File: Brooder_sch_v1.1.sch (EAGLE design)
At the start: 30 parts, among them J1 DCJ0202, J2 1X2-3.5MM, U1 328P

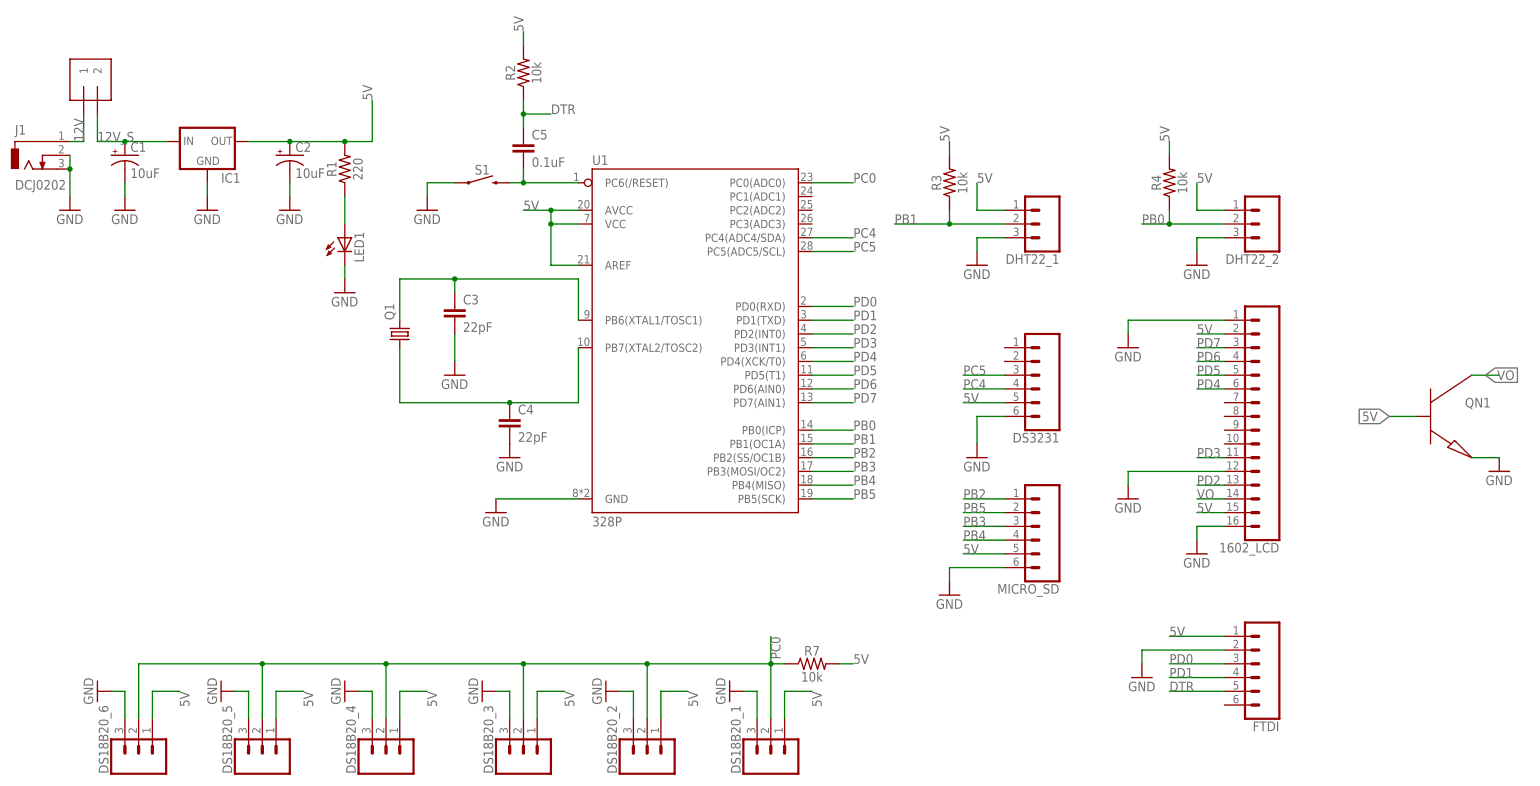
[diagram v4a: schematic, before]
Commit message: Adds test led
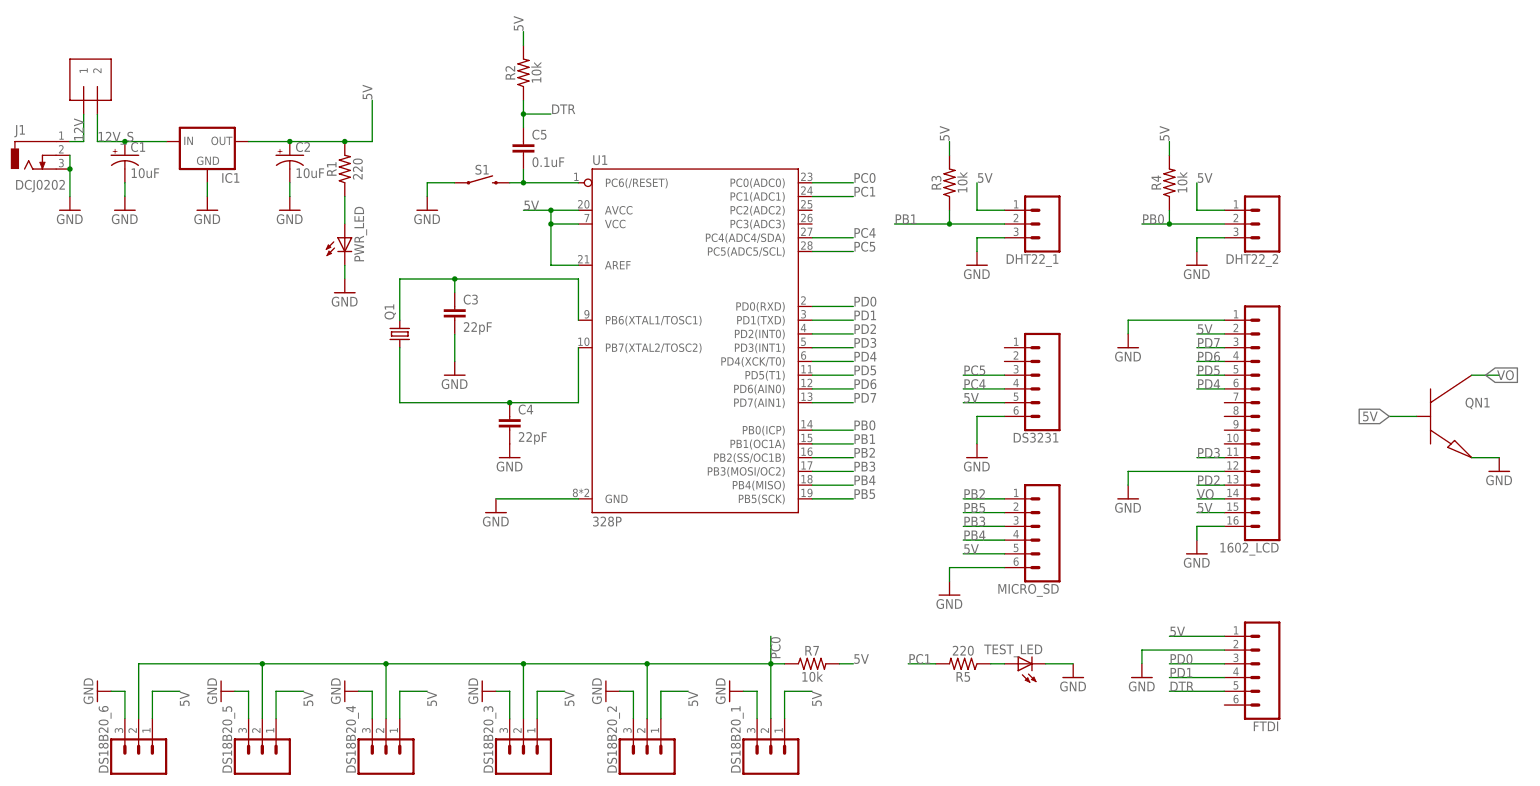
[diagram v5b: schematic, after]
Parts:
- added R5: 220, SparkFun-Resistors:10MOHM-HORIZ-1/4W-5%
- added TEST_LED: (no value), adafruit:LED5MM
- renumbered LED1 to PWR_LED
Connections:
- new net N$1: R5.1, TEST_LED.A
- new net PC1: R5.2, U1.PC1(ADC1)
- net GND: now also TEST_LED.C
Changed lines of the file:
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@@
 <part name="IC1" library="v-reg" library_urn="urn:adsk.eagle:library:409" deviceset="78XXS" device="" package3d_urn="urn:adsk.eagle:package:30342/1"/>
 <part name="R1" library="SparkFun-Resistors" deviceset="10MOHM" device="-HORIZ-1/4W-5%" value="220"/>
-<part name="LED1" library="adafruit" deviceset="LED" device="5MM"/>
+<part name="PWR_LED" library="adafruit" deviceset="LED" device="5MM"/>
 <part name="U1" library="SparkFun-IC-Microcontroller" deviceset="ATMEGA328P_PDIP" device="" value="328P"/>
 <part name="Q1" library="adafruit" deviceset="CRYSTAL" device="HC49S"/>
@@
 <part name="DS3231" library="SparkFun-Connectors" deviceset="CONN_06" device="NO_SILK_FEMALE_PTH"/>
 <part name="GND24" library="supply1" library_urn="urn:adsk.eagle:library:371" deviceset="GND" device=""/>
+<part name="R5" library="SparkFun-Resistors" deviceset="10MOHM" device="-HORIZ-1/4W-5%" value="220"/>
+<part name="TEST_LED" library="adafruit" deviceset="LED" device="5MM"/>
+<part name="GND25" library="supply1" library_urn="urn:adsk.eagle:library:371" deviceset="GND" device=""/>
 </parts>
 <sheets>
@@
 <attribute name="VALUE" x="-8.636" y="106.68" size="1.778" layer="96" font="vector" rot="R90" align="top-center"/>
 </instance>
-<instance part="LED1" gate="G$1" x="-10.16" y="93.98" smashed="yes">
+<instance part="PWR_LED" gate="G$1" x="-10.16" y="93.98" smashed="yes">
 <attribute name="NAME" x="-6.604" y="89.408" size="1.778" layer="95" rot="R90"/>
 <attribute name="VALUE" x="-4.445" y="89.408" size="1.778" layer="96" rot="R90"/>
@@
 <instance part="GND24" gate="1" x="106.68" y="53.34" smashed="yes">
 <attribute name="VALUE" x="104.14" y="50.8" size="1.778" layer="96"/>
+</instance>
+<instance part="R5" gate="G$1" x="104.14" y="15.24" smashed="yes" rot="R180">
+<attribute name="NAME" x="104.14" y="13.716" size="1.778" layer="95" font="vector" rot="R180" align="bottom-center"/>
+<attribute name="VALUE" x="104.14" y="16.764" size="1.778" layer="96" font="vector" rot="R180" align="top-center"/>
+</instance>
+<instance part="TEST_LED" gate="G$1" x="114.3" y="15.24" smashed="yes" rot="R90">
+<attribute name="NAME" x="118.872" y="18.796" size="1.778" layer="95" rot="R180"/>
+<attribute name="VALUE" x="118.872" y="20.955" size="1.778" layer="96" rot="R180"/>
+</instance>
+<instance part="GND25" gate="1" x="124.46" y="12.7" smashed="yes">
+<attribute name="VALUE" x="121.92" y="10.16" size="1.778" layer="96"/>
 </instance>
 </instances>
@@
 </segment>
 <segment>
-<pinref part="LED1" gate="G$1" pin="C"/>
+<pinref part="PWR_LED" gate="G$1" pin="C"/>
 <pinref part="GND5" gate="1" pin="GND"/>
 <wire x1="-10.16" y1="88.9" x2="-10.16" y2="86.36" width="0.1524" layer="91"/>
@@
 <wire x1="106.68" y1="60.96" x2="106.68" y2="55.88" width="0.1524" layer="91"/>
 <pinref part="GND24" gate="1" pin="GND"/>
+</segment>
+<segment>
+<pinref part="TEST_LED" gate="G$1" pin="C"/>
+<pinref part="GND25" gate="1" pin="GND"/>
+<wire x1="119.38" y1="15.24" x2="124.46" y2="15.24" width="0.1524" layer="91"/>
 </segment>
 </net>
@@
 <segment>
 <pinref part="R1" gate="G$1" pin="1"/>
-<pinref part="LED1" gate="G$1" pin="A"/>
+<pinref part="PWR_LED" gate="G$1" pin="A"/>
 <wire x1="-10.16" y1="101.6" x2="-10.16" y2="96.52" width="0.1524" layer="91"/>
 </segment>
@@
 </segment>
 </net>
+<net name="N$1" class="0">
+<segment>
+<pinref part="R5" gate="G$1" pin="1"/>
+<pinref part="TEST_LED" gate="G$1" pin="A"/>
+<wire x1="109.22" y1="15.24" x2="111.76" y2="15.24" width="0.1524" layer="91"/>
+</segment>
+</net>
+<net name="PC1" class="0">
+<segment>
+<pinref part="R5" gate="G$1" pin="2"/>
+<wire x1="99.06" y1="15.24" x2="93.98" y2="15.24" width="0.1524" layer="91"/>
+<label x="93.98" y="15.24" size="1.778" layer="95"/>
+</segment>
+<segment>
+<pinref part="U1" gate="U1" pin="PC1(ADC1)"/>
+<wire x1="76.2" y1="101.6" x2="83.82" y2="101.6" width="0.1524" layer="91"/>
+<label x="83.82" y="101.6" size="1.778" layer="95"/>
+</segment>
+</net>

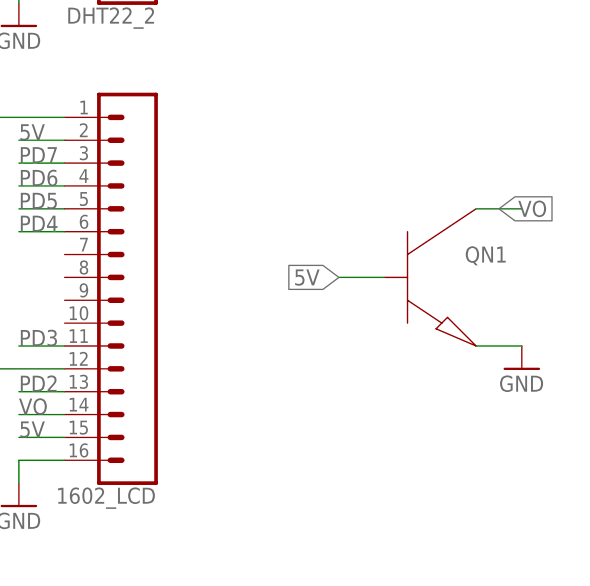
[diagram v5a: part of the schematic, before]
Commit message: Adds actual pot symbol
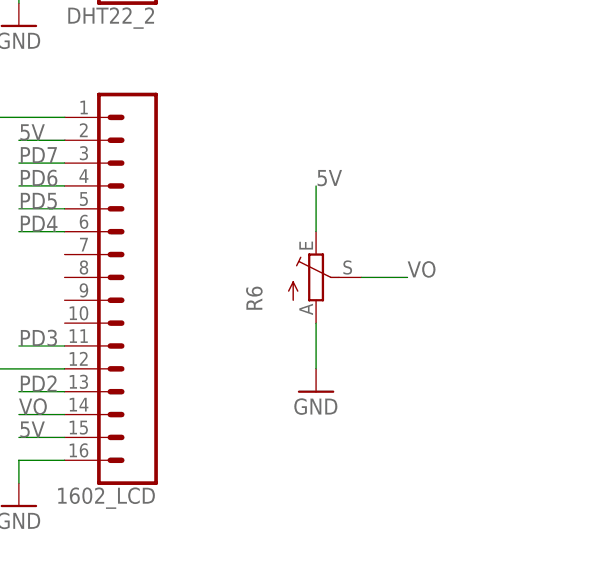
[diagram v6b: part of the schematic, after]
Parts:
- removed QN1: (no value), sym:NPN
- added R6: (no value), pot:TRIM_EU-RJ6
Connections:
- net 5V: now also R6.E; no longer QN1.B
- net GND: now also R6.A; no longer QN1.E
- net VO: now also R6.S; no longer QN1.C
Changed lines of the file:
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@@
 <part name="GND14" library="supply1" library_urn="urn:adsk.eagle:library:371" deviceset="GND" device=""/>
 <part name="GND15" library="supply1" library_urn="urn:adsk.eagle:library:371" deviceset="GND" device=""/>
-<part name="QN1" library="sym" deviceset="NPN" device=""/>
-<part name="GND16" library="supply1" library_urn="urn:adsk.eagle:library:371" deviceset="GND" device=""/>
 <part name="MICRO_SD" library="SparkFun-Connectors" deviceset="CONN_06" device="NO_SILK_FEMALE_PTH"/>
 <part name="GND17" library="supply1" library_urn="urn:adsk.eagle:library:371" deviceset="GND" device=""/>
@@
 <part name="TEST_LED" library="adafruit" deviceset="LED" device="5MM"/>
 <part name="GND25" library="supply1" library_urn="urn:adsk.eagle:library:371" deviceset="GND" device=""/>
+<part name="R6" library="pot" library_urn="urn:adsk.eagle:library:331" deviceset="TRIM_EU-" device="RJ6" package3d_urn="urn:adsk.eagle:package:22699/1"/>
+<part name="GND26" library="supply1" library_urn="urn:adsk.eagle:library:371" deviceset="GND" device=""/>
 </parts>
 <sheets>
@@
 <attribute name="VALUE" x="132.08" y="71.12" size="1.778" layer="96"/>
 </instance>
-<instance part="QN1" gate="G$1" x="187.96" y="68.58" smashed="yes">
-<attribute name="NAME" x="196.85" y="63.5" size="1.778" layer="95" align="center-left"/>
-<attribute name="VALUE" x="196.85" y="57.785" size="1.778" layer="96" align="center-left"/>
-</instance>
-<instance part="GND16" gate="1" x="203.2" y="50.8" smashed="yes">
-<attribute name="VALUE" x="200.66" y="48.26" size="1.778" layer="96"/>
-</instance>
 <instance part="MICRO_SD" gate="G$1" x="116.84" y="40.64" smashed="yes" rot="R180">
 <attribute name="VALUE" x="121.92" y="50.546" size="1.778" layer="96" font="vector" rot="R180"/>
@@
 <instance part="GND25" gate="1" x="124.46" y="12.7" smashed="yes">
 <attribute name="VALUE" x="121.92" y="10.16" size="1.778" layer="96"/>
+</instance>
+<instance part="R6" gate="1" x="180.34" y="60.96"/>
+<instance part="GND26" gate="1" x="180.34" y="48.26" smashed="yes">
+<attribute name="VALUE" x="177.8" y="45.72" size="1.778" layer="96"/>
 </instance>
 </instances>
@@
 </segment>
 <segment>
-<pinref part="QN1" gate="G$1" pin="E"/>
-<wire x1="198.12" y1="53.34" x2="203.2" y2="53.34" width="0.1524" layer="91"/>
-<pinref part="GND16" gate="1" pin="GND"/>
-</segment>
-<segment>
 <pinref part="MICRO_SD" gate="G$1" pin="6"/>
 <wire x1="111.76" y1="33.02" x2="101.6" y2="33.02" width="0.1524" layer="91"/>
@@
 <pinref part="GND25" gate="1" pin="GND"/>
 <wire x1="119.38" y1="15.24" x2="124.46" y2="15.24" width="0.1524" layer="91"/>
+</segment>
+<segment>
+<pinref part="R6" gate="1" pin="A"/>
+<wire x1="180.34" y1="55.88" x2="180.34" y2="50.8" width="0.1524" layer="91"/>
+<pinref part="GND26" gate="1" pin="GND"/>
 </segment>
 </net>
@@
 </segment>
 <segment>
-<pinref part="QN1" gate="G$1" pin="B"/>
-<wire x1="187.96" y1="60.96" x2="182.88" y2="60.96" width="0.1524" layer="91"/>
-<label x="182.88" y="60.96" size="1.778" layer="95" rot="R180" xref="yes"/>
-</segment>
-<segment>
 <pinref part="MICRO_SD" gate="G$1" pin="5"/>
 <wire x1="111.76" y1="35.56" x2="104.14" y2="35.56" width="0.1524" layer="91"/>
@@
 <wire x1="111.76" y1="63.5" x2="104.14" y2="63.5" width="0.1524" layer="91"/>
 <label x="104.14" y="63.5" size="1.778" layer="95"/>
+</segment>
+<segment>
+<pinref part="R6" gate="1" pin="E"/>
+<wire x1="180.34" y1="66.04" x2="180.34" y2="71.12" width="0.1524" layer="91"/>
+<label x="180.34" y="71.12" size="1.778" layer="95"/>
 </segment>
 </net>
@@
 </segment>
 <segment>
-<pinref part="QN1" gate="G$1" pin="C"/>
-<label x="200.66" y="68.58" size="1.778" layer="95" xref="yes"/>
-<wire x1="198.12" y1="68.58" x2="203.2" y2="68.58" width="0.1524" layer="91"/>
-</segment>
-</net>
+<pinref part="R6" gate="1" pin="S"/>
+<wire x1="185.42" y1="60.96" x2="190.5" y2="60.96" width="0.1524" layer="91"/>
+<label x="190.5" y="60.96" size="1.778" layer="95"/>
+</segment>
+</net>
